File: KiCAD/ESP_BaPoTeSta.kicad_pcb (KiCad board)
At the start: 2 copper layers, 39.4 x 49.5 mm, 20 parts, among them P1 Progr, P2 Battery, P3 Power, SW1 Upload, SW2 Reset, U1 MCP1700-3302E, U2 ESP-12, U3 DS18B20

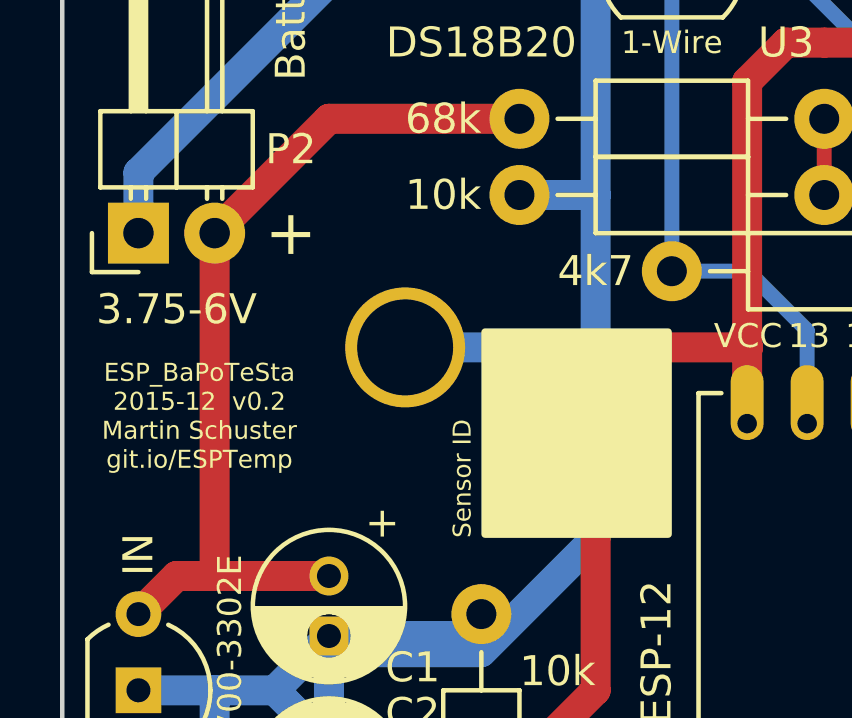
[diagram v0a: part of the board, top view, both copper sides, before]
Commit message: ENH: bigger SensorID field on F.SilkS
by moving the 1st mounting hole NW
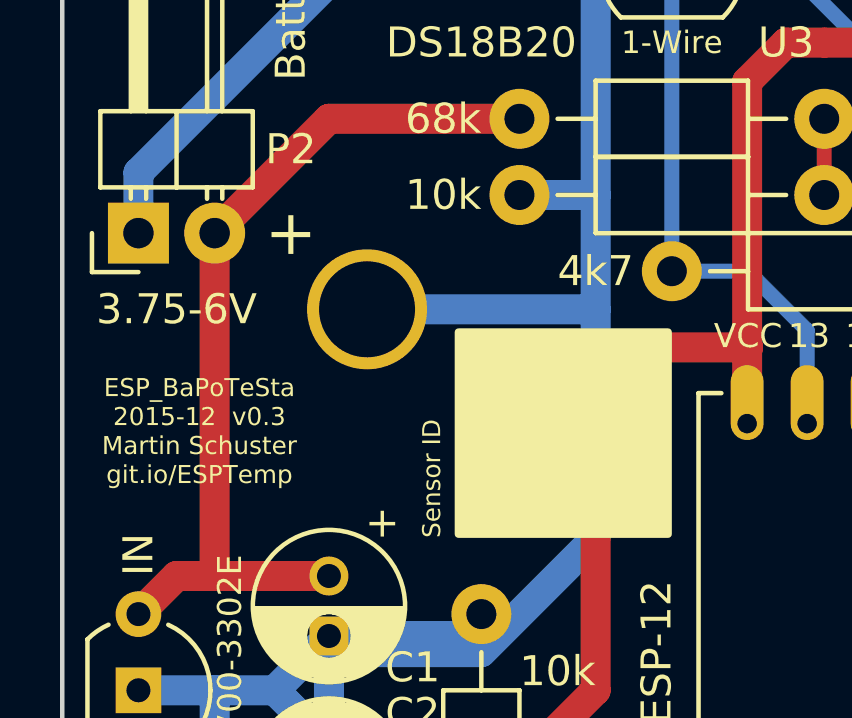
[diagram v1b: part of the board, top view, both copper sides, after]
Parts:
- moved REF** 1.80 mm to (115.6, 80.0)
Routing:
- net GND: track 136.3 -> 137.6 mm
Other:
- board text added: "ESP_BaPoTeSta 2015-12 v0.3 Martin Schuster git.io/ESPTemp"
- board text removed: "ESP_BaPoTeSta 2015-12 v0.2 Martin Schuster git.io/ESPTemp"
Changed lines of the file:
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@@
     (thickness 1.6)
     (drawings 56)
-    (tracks 108)
+    (tracks 109)
     (zones 0)
     (modules 20)
@@
     (visible_elements FFFFFF7F)
     (pcbplotparams
-      (layerselection 0x010e0_80000001)
+      (layerselection 0x010f0_80000001)
       (usegerberextensions true)
       (excludeedgelayer true)
@@
   )
   (module Mounting_Holes:MountingHole_2-5mm (layer F.Cu)
-    (at 116.84 81.28)
+    (at 115.57 80.01)
     (descr "Mounting hole, Befestigungsbohrung, 2,5mm, No Annular, Kein Restring,")
     (tags "Mounting hole, Befestigungsbohrung, 2,5mm, No Annular, Kein Restring,")
@@
     (effects (font (size 0.8 0.8) (thickness 0.16)) (justify mirror))
   )
-  (gr_text "Sensor ID" (at 118.745 87.63 90) (layer F.SilkS)
+  (gr_text "Sensor ID" (at 117.729 87.63 90) (layer F.SilkS)
     (effects (font (size 0.6 0.6) (thickness 0.1)) (justify left))
   )
@@
     (effects (font (size 1.5 1.5) (thickness 0.3)))
   )
-  (gr_text "ESP_BaPoTeSta\n2015-12  v0.2\nMartin Schuster\ngit.io/ESPTemp" (at 109.982 83.566) (layer F.SilkS)
+  (gr_text "ESP_BaPoTeSta\n2015-12  v0.3\nMartin Schuster\ngit.io/ESPTemp" (at 109.982 84.074) (layer F.SilkS)
     (effects (font (size 0.6 0.6) (thickness 0.1)))
   )
@@
   (segment (start 120.65 73.66) (end 118.11 73.66) (width 1) (layer F.Cu) (net 1))
   (segment (start 107.95 90.17) (end 109.22 88.9) (width 1) (layer F.Cu) (net 1))
+  (segment (start 123.19 80.01) (end 123.19 76.2) (width 1) (layer B.Cu) (net 2))
+  (segment (start 123.19 81.28) (end 123.19 80.01) (width 1) (layer B.Cu) (net 2))
+  (segment (start 123.19 80.01) (end 115.57 80.01) (width 1) (layer B.Cu) (net 2))
   (segment (start 123.19 87.63) (end 123.19 81.28) (width 1) (layer B.Cu) (net 2))
-  (segment (start 123.19 81.28) (end 123.19 76.2) (width 1) (layer B.Cu) (net 2))
-  (segment (start 116.84 81.28) (end 123.19 81.28) (width 1) (layer B.Cu) (net 2))
   (segment (start 107.95 102.87) (end 110.49 100.33) (width 1) (layer B.Cu) (net 2))
   (segment (start 110.49 100.33) (end 110.49 99.06) (width 1) (layer B.Cu) (net 2))
@@
     (polygon
       (pts
-        (xy 119.38 80.645) (xy 125.73 80.645) (xy 125.73 87.63) (xy 119.38 87.63)
+        (xy 118.491 80.645) (xy 125.73 80.645) (xy 125.73 87.63) (xy 118.491 87.63)
       )
     )

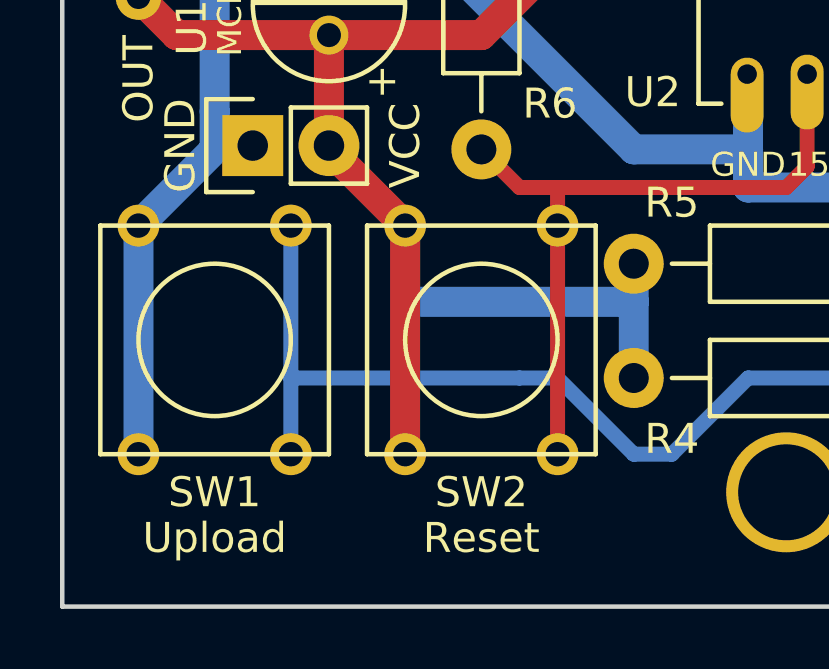
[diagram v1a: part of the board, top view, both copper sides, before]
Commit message: ENH: Move buttons closer to the edge of the PCB
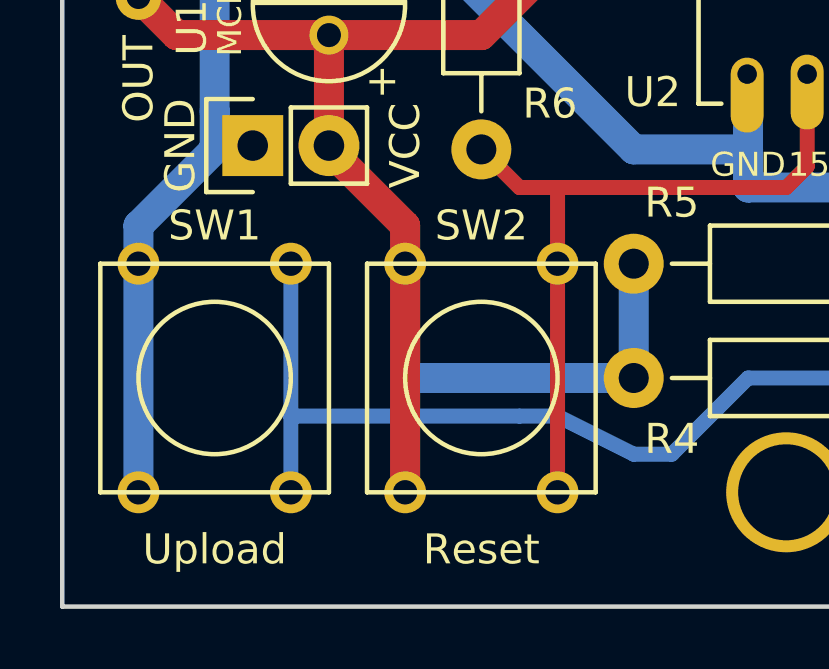
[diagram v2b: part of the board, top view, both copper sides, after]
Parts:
- moved SW1 1.27 mm to (110.5, 108.0)
- moved SW2 1.27 mm to (119.4, 108.0)
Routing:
- net VCC: track 81.8 -> 84.4 mm
- net GND: track 137.6 -> 138.8 mm
- net Net-(R6-Pad2): track 23.6 -> 24.9 mm
- net Net-(R4-Pad1): track 43.7 -> 43.0 mm
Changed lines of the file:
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@@
     (thickness 1.6)
     (drawings 56)
-    (tracks 109)
+    (tracks 110)
     (zones 0)
     (modules 20)
@@
   )
   (module Buttons_Switches_ThroughHole:SW_PUSH_SMALL (layer F.Cu)
-    (at 110.49 106.68 270)
-    (fp_text reference SW1 (at 5.08 0 360) (layer F.SilkS)
-      (effects (font (size 1 1) (thickness 0.15)))
-    )
-    (fp_text value Upload (at 6.604 0 360) (layer F.SilkS)
+    (at 110.49 107.95 270)
+    (fp_text reference SW1 (at -5.08 0 360) (layer F.SilkS)
+      (effects (font (size 1 1) (thickness 0.15)))
+    )
+    (fp_text value Upload (at 5.715 0 360) (layer F.SilkS)
       (effects (font (size 1 1) (thickness 0.15)))
     )
@@
   )
   (module Buttons_Switches_ThroughHole:SW_PUSH_SMALL (layer F.Cu)
-    (at 119.38 106.68 270)
-    (fp_text reference SW2 (at 5.08 0 360) (layer F.SilkS)
-      (effects (font (size 1 1) (thickness 0.15)))
-    )
-    (fp_text value Reset (at 6.604 0 360) (layer F.SilkS)
+    (at 119.38 107.95 270)
+    (fp_text reference SW2 (at -5.08 0 360) (layer F.SilkS)
+      (effects (font (size 1 1) (thickness 0.15)))
+    )
+    (fp_text value Reset (at 5.715 0 360) (layer F.SilkS)
       (effects (font (size 1 1) (thickness 0.15)))
     )
@@
   (segment (start 110.49 100.33) (end 110.49 99.06) (width 1) (layer B.Cu) (net 2))
   (segment (start 110.49 99.06) (end 110.49 92.71) (width 1) (layer B.Cu) (net 2))
-  (segment (start 107.95 110.49) (end 107.95 102.87) (width 1) (layer B.Cu) (net 2))
+  (segment (start 107.95 111.76) (end 107.95 102.87) (width 1) (layer B.Cu) (net 2))
   (segment (start 123.19 68.58) (end 114.824 68.58) (width 1) (layer B.Cu) (net 2))
   (segment (start 114.824 68.58) (end 107.95 75.454) (width 1) (layer B.Cu) (net 2))
@@
   (segment (start 112.49 92.71) (end 114.3 90.9) (width 1) (layer B.Cu) (net 2))
   (segment (start 119.38 90.17) (end 118.65 90.9) (width 1) (layer B.Cu) (net 2))
+  (segment (start 116.84 104.14) (end 116.84 102.87) (width 1) (layer F.Cu) (net 3))
   (segment (start 116.84 102.87) (end 114.3 100.33) (width 1) (layer F.Cu) (net 3))
-  (segment (start 116.84 105.41) (end 116.84 102.87) (width 1) (layer B.Cu) (net 3))
-  (segment (start 124.46 105.41) (end 124.46 104.14) (width 1) (layer B.Cu) (net 3))
-  (segment (start 124.46 107.95) (end 124.46 105.41) (width 1) (layer B.Cu) (net 3))
-  (segment (start 124.46 105.41) (end 116.84 105.41) (width 1) (layer B.Cu) (net 3))
+  (segment (start 116.84 107.95) (end 116.84 104.14) (width 1) (layer B.Cu) (net 3))
+  (segment (start 124.46 107.95) (end 124.46 104.14) (width 1) (layer B.Cu) (net 3))
+  (segment (start 124.46 107.95) (end 124.46 107.95) (width 1) (layer B.Cu) (net 3))
+  (segment (start 124.46 107.95) (end 116.84 107.95) (width 1) (layer B.Cu) (net 3))
   (segment (start 114.3 100.33) (end 114.3 96.52) (width 1) (layer F.Cu) (net 3))
-  (segment (start 116.84 110.49) (end 116.84 102.87) (width 1) (layer F.Cu) (net 3))
+  (segment (start 116.84 111.76) (end 116.84 104.14) (width 1) (layer F.Cu) (net 3))
   (segment (start 128.24 81.28) (end 123.19 81.28) (width 1) (layer F.Cu) (net 3))
   (segment (start 119.38 96.52) (end 123.19 92.71) (width 1) (layer F.Cu) (net 3))
@@
   (segment (start 142.022102 77.252102) (end 142.24 77.47) (width 0.5) (layer F.Cu) (net 7))
   (segment (start 142.24 77.47) (end 142.24 83.82) (width 0.5) (layer F.Cu) (net 7))
-  (segment (start 120.65 107.95) (end 113.03 107.95) (width 0.5) (layer B.Cu) (net 8))
+  (segment (start 120.65 109.22) (end 113.03 109.22) (width 0.5) (layer B.Cu) (net 8))
   (segment (start 134.62 107.95) (end 128.27 107.95) (width 0.5) (layer B.Cu) (net 8))
-  (segment (start 121.92 107.95) (end 120.65 107.95) (width 0.5) (layer B.Cu) (net 8))
+  (segment (start 121.92 109.22) (end 120.65 109.22) (width 0.5) (layer B.Cu) (net 8))
   (segment (start 128.27 107.95) (end 125.73 110.49) (width 0.5) (layer B.Cu) (net 8))
   (segment (start 125.73 110.49) (end 124.46 110.49) (width 0.5) (layer B.Cu) (net 8))
-  (segment (start 124.46 110.49) (end 121.92 107.95) (width 0.5) (layer B.Cu) (net 8))
-  (segment (start 113.03 102.87) (end 113.03 107.95) (width 0.5) (layer B.Cu) (net 8))
-  (segment (start 113.03 107.95) (end 113.03 110.49) (width 0.5) (layer B.Cu) (net 8))
+  (segment (start 124.46 110.49) (end 121.92 109.22) (width 0.5) (layer B.Cu) (net 8))
+  (segment (start 113.03 104.14) (end 113.03 109.22) (width 0.5) (layer B.Cu) (net 8))
+  (segment (start 113.03 109.22) (end 113.03 111.76) (width 0.5) (layer B.Cu) (net 8))
   (segment (start 134.62 107.95) (end 137.16 105.41) (width 0.5) (layer F.Cu) (net 8))
   (segment (start 137.16 102.87) (end 134.24 99.95) (width 0.5) (layer F.Cu) (net 8))
@@
   (segment (start 134.62 104.14) (end 132.24 101.76) (width 0.5) (layer F.Cu) (net 9))
   (segment (start 132.24 101.76) (end 132.24 97.82) (width 0.5) (layer F.Cu) (net 9))
+  (segment (start 121.92 104.14) (end 121.92 101.6) (width 0.5) (layer F.Cu) (net 10))
   (segment (start 120.65 101.6) (end 121.92 101.6) (width 0.5) (layer F.Cu) (net 10))
   (segment (start 121.92 101.6) (end 129.54 101.6) (width 0.5) (layer F.Cu) (net 10))
-  (segment (start 121.92 102.87) (end 121.92 101.6) (width 0.5) (layer F.Cu) (net 10))
-  (segment (start 121.92 110.49) (end 121.92 102.87) (width 0.5) (layer F.Cu) (net 10))
+  (segment (start 121.92 111.76) (end 121.92 104.14) (width 0.5) (layer F.Cu) (net 10))
   (segment (start 120.65 101.6) (end 119.38 100.33) (width 0.5) (layer F.Cu) (net 10))
   (segment (start 129.54 101.6) (end 130.24 100.9) (width 0.5) (layer F.Cu) (net 10))

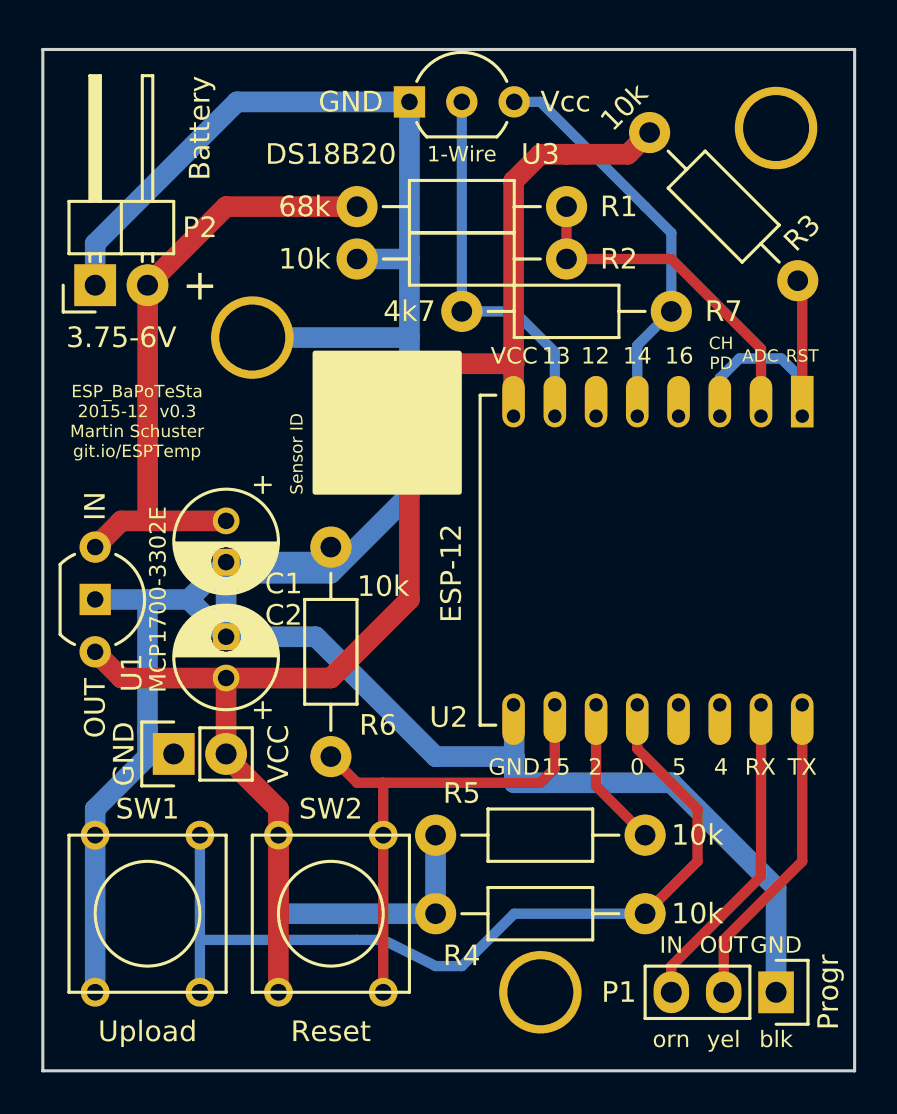
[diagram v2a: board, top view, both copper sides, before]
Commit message: WIP: Redesign PCB
Use SMD resistors, and start to work on #14, #15 and #16
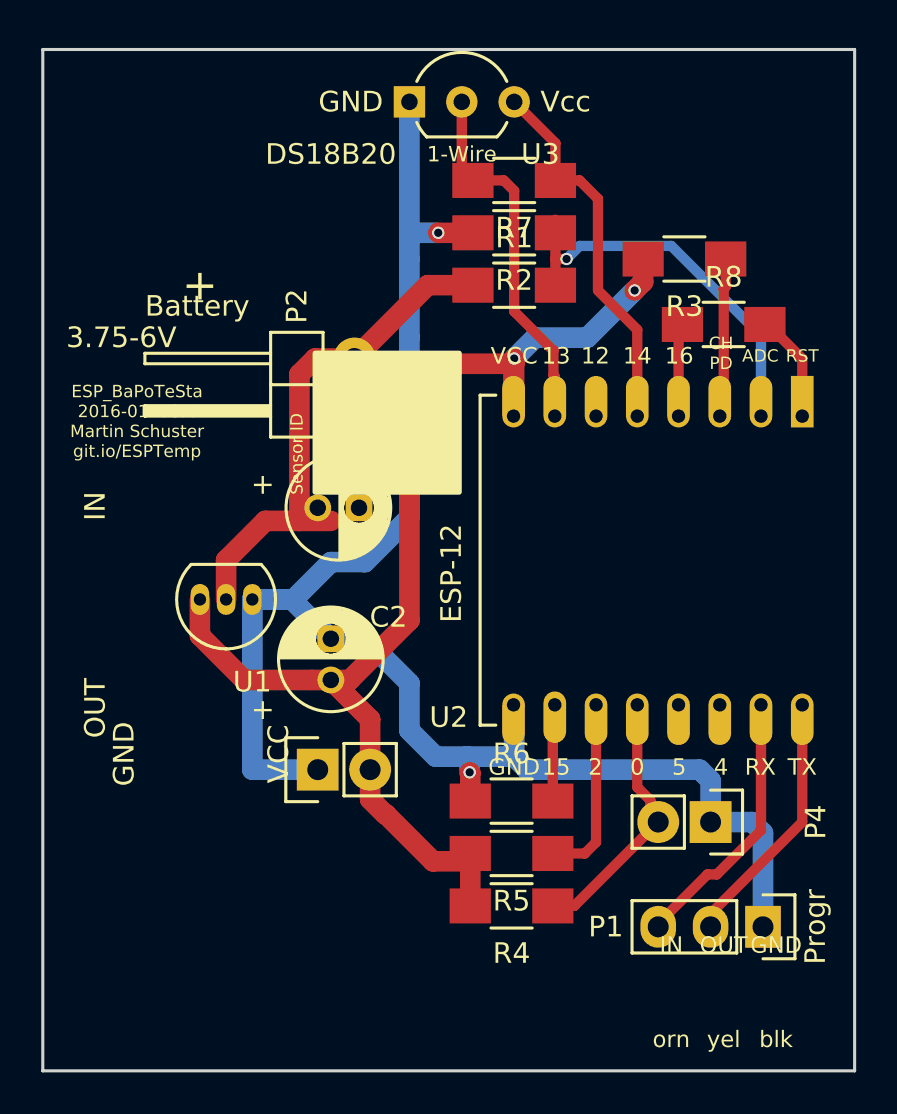
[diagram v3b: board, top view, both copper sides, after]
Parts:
- removed REF** (x3): MountingHole_2-5mm, Mounting_Holes:MountingHole_2-5mm
- removed SW1: Upload, Buttons_Switches_ThroughHole:SW_PUSH_SMALL
- removed SW2: Reset, Buttons_Switches_ThroughHole:SW_PUSH_SMALL
- added P4: Upload, Pin_Headers:Pin_Header_Straight_1x02, F.Cu at (137.8, 103.5)
- added R8: 10k, Resistors_SMD:R_1206_HandSoldering, F.Cu at (138.4, 79.4)
- R1, R2, R3, R4, R5, R6, R7: footprint Resistors_ThroughHole:Resistor_Horizontal_RM10mm -> Resistors_SMD:R_1206_HandSoldering
- U1: value MCP1700-3302E -> MCP1700-330; footprint TO_SOT_Packages_THT:TO-92_Inline_Wide -> TO_SOT_Packages_THT:TO-92_Inline_Narrow_Oval
- moved P2 14.0 mm to (120.5, 83.6), turned to 180 degrees
- moved R6 11.4 mm to (128.1, 102.5), turned to 0 degrees
- moved U1 8.03 mm to (115.6, 92.7), turned to 180 degrees
- moved P3 7.03 mm to (118.7, 101.0)
- moved R7 6.84 mm to (128.3, 72.4)
- moved C2 5.08 mm to (119.4, 96.6)
- moved R1 4.58 mm to (128.3, 77.5)
- moved C1 4.49 mm to (118.7, 88.3), turned to 0 degrees
- moved P1 3.24 mm to (140.3, 108.6)
- moved R3 3.18 mm to (136.5, 76.2), turned to 180 degrees
- moved R2 2.84 mm to (128.3, 74.9)
- moved R5 1.66 mm to (128.1, 105.0)
- moved R4 1.45 mm to (128.1, 107.6)
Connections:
- U1 pad 1: +BATT -> GND
- U1 pad 2: GND -> +BATT
- U2 pad 1: Net-(R3-Pad1) -> Net-(R8-Pad2)
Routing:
- net GND: track 138.8 -> 87.9 mm, vias 0 -> 2
- net Net-(P4-Pad2): track 43.0 -> 12.6 mm
- net VCC: track 84.4 -> 61.0 mm, vias 0 -> 2
- net Net-(R6-Pad2): track 24.9 -> 4.80 mm
- net Net-(R3-Pad1): track 15.1 -> 7.74 mm
- net Net-(R8-Pad2): track 0.00 -> 5.28 mm
- net +BATT: track 30.0 -> 25.1 mm
- net Net-(R8-Pad1): track 0.00 -> 4.71 mm
- net Net-(P1-Pad2): track 15.5 -> 12.6 mm
- net Net-(P1-Pad3): track 15.7 -> 13.1 mm
- net Net-(R5-Pad1): track 7.31 -> 8.99 mm
- net Net-(R1-Pad2): track 17.0 -> 18.6 mm, vias 0 -> 1
- net /Pwr1W: track 19.9 -> 18.4 mm
- net /1Wire: track 18.6 -> 18.0 mm
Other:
- board text added: "ESP_BaPoTeSta 2016-01 v0.4 Martin Schuster git.io/ESPTemp"
- board text removed: "ESP_BaPoTeSta 2015-12 v0.3 Martin Schuster git.io/ESPTemp"

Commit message: WIP: Continue improving PCB
continue the work started in 0493dcc
add additional header to enter config mode
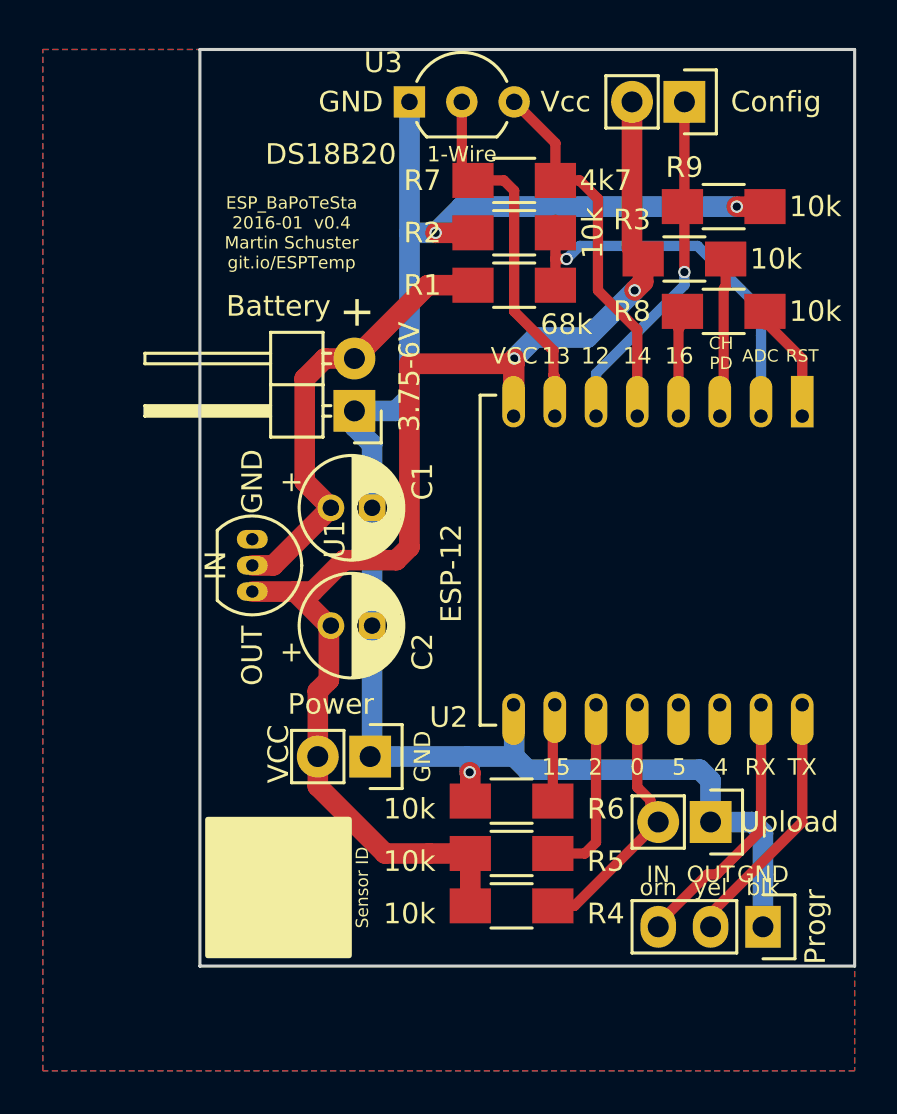
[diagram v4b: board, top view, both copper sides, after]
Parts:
- added P5: Config, Pin_Headers:Pin_Header_Straight_1x02, F.Cu at (136.5, 68.6)
- added R9: 10k, Resistors_SMD:R_1206_HandSoldering, F.Cu at (138.4, 73.7)
- moved U1 2.92 mm to (115.6, 89.8), turned to 270 degrees
- moved C2 2.63 mm to (119.4, 94.0), turned to 0 degrees
- moved P3 2.62 mm to (121.3, 100.3), turned to 270 degrees
- moved R8 0.64 mm to (138.4, 78.7)
- moved C1 0.63 mm to (119.4, 88.3)
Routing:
- net Net-(P5-Pad1): track 0.00 -> 17.1 mm, vias 0 -> 1
- net VCC: track 61.0 -> 66.2 mm
- net +BATT: track 25.1 -> 21.8 mm
- net GND: track 87.9 -> 85.1 mm, vias 2 -> 3
- net Net-(R1-Pad2): track 18.6 -> 19.4 mm
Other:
- board size 39.4 x 49.5 mm -> 31.8 x 44.4 mm
